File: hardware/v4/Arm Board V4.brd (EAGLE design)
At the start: 108 x 50.8 mm, 38 parts, among them IC3 L6206D, P1 STELLARIS-LAUNCHPADSTELLARIS-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, U1 SN74LS241DW, U2 XBEE-1B3

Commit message: cleaned up robo arm a bit
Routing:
- net A1: track 31.0 -> 31.9 mm
- net GND: track 16.8 -> 17.6 mm, vias 8 -> 10
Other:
- board text added: "5V"
- board text added: "GND"
- board text added: "RX3"
- board text added: "TX3"
- board text removed: "GND 5V RX3 TX3"

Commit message: added cap
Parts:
- added C1: (no value), SparkFun-Capacitors:PANASONIC_E
- moved JP11 2.54 mm to (86.8, 46.2)
- moved JP12 2.54 mm to (98.3, 46.2)
- moved JP10 2.54 mm to (92.6, 46.2)
- moved U$7 1.37 mm to (66.0, 46.4)
- moved JP9 0.78 mm to (79.2, 46.6), turned to 180 degrees
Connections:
- net +12V: now also C1.+
- net GND: now also C1.-
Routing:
- net DDATA_1: track 108.3 -> 84.0 mm
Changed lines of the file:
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@@
 </element>
 <element name="U2" library="SparkFun" package="XBEE-SMD" value="XBEE-1B3" x="59.37" y="0"/>
-<element name="JP9" library="MRDT-2015-Arm" package="DYNAMIXEL-1X03" value="DYNAMIXEL-1X03" x="78.58125" y="46.19625" smashed="yes" rot="R270">
-<attribute name="NAME" x="80.41005" y="47.54245" size="1.27" layer="25" ratio="10" rot="R270" display="off"/>
-<attribute name="VALUE" x="75.40625" y="47.46625" size="1.27" layer="27" rot="R270"/>
-</element>
-<element name="JP10" library="MRDT-2015-Arm" package="DYNAMIXEL-1X03" value="DYNAMIXEL-1X03" x="90.01125" y="46.19625" smashed="yes" rot="R270">
-<attribute name="NAME" x="91.84005" y="47.54245" size="1.27" layer="25" ratio="10" rot="R270" display="off"/>
-<attribute name="VALUE" x="86.83625" y="47.46625" size="1.27" layer="27" rot="R270"/>
-</element>
-<element name="JP11" library="MRDT-2015-Arm" package="DYNAMIXEL-1X03" value="DYNAMIXEL-1X03" x="84.29625" y="46.19625" smashed="yes" rot="R270">
-<attribute name="NAME" x="86.12505" y="47.54245" size="1.27" layer="25" ratio="10" rot="R270" display="off"/>
-<attribute name="VALUE" x="81.12125" y="47.46625" size="1.27" layer="27" rot="R270"/>
-</element>
-<element name="JP12" library="MRDT-2015-Arm" package="DYNAMIXEL-1X03" value="DYNAMIXEL-1X03" x="95.72625" y="46.19625" smashed="yes" rot="R270">
-<attribute name="NAME" x="97.55505" y="47.54245" size="1.27" layer="25" ratio="10" rot="R270" display="off"/>
-<attribute name="VALUE" x="92.55125" y="47.46625" size="1.27" layer="27" rot="R270"/>
+<element name="JP9" library="MRDT-2015-Arm" package="DYNAMIXEL-1X03" value="DYNAMIXEL-1X03" x="79.21625" y="46.64075" smashed="yes" rot="R180">
+<attribute name="NAME" x="80.56245" y="44.81195" size="1.27" layer="25" ratio="10" rot="R180" display="off"/>
+<attribute name="VALUE" x="80.48625" y="49.81575" size="1.27" layer="27" rot="R180"/>
+</element>
+<element name="JP10" library="MRDT-2015-Arm" package="DYNAMIXEL-1X03" value="DYNAMIXEL-1X03" x="92.55125" y="46.19625" smashed="yes" rot="R270">
+<attribute name="NAME" x="94.38005" y="47.54245" size="1.27" layer="25" ratio="10" rot="R270" display="off"/>
+<attribute name="VALUE" x="89.37625" y="47.46625" size="1.27" layer="27" rot="R270"/>
+</element>
+<element name="JP11" library="MRDT-2015-Arm" package="DYNAMIXEL-1X03" value="DYNAMIXEL-1X03" x="86.83625" y="46.19625" smashed="yes" rot="R270">
+<attribute name="NAME" x="88.66505" y="47.54245" size="1.27" layer="25" ratio="10" rot="R270" display="off"/>
+<attribute name="VALUE" x="83.66125" y="47.46625" size="1.27" layer="27" rot="R270"/>
+</element>
+<element name="JP12" library="MRDT-2015-Arm" package="DYNAMIXEL-1X03" value="DYNAMIXEL-1X03" x="98.26625" y="46.19625" smashed="yes" rot="R270">
+<attribute name="NAME" x="100.09505" y="47.54245" size="1.27" layer="25" ratio="10" rot="R270" display="off"/>
+<attribute name="VALUE" x="95.09125" y="47.46625" size="1.27" layer="27" rot="R270"/>
 </element>
 <element name="P1" library="StellarisLaunchPad_Fred" package="LAUNCHPAD-XL" value="STELLARIS-LAUNCHPADSTELLARIS-LAUNCHPAD-XL" x="-21.59" y="0"/>
@@
 <element name="S3" library="SparkFun-Electromechanical" package="STANDOFF-ELECTRICAL" value="STANDOFF_ELECTRICAL" x="100.33" y="8.89" rot="MR0"/>
 <element name="S4" library="SparkFun-Electromechanical" package="STANDOFF-ELECTRICAL" value="STANDOFF_ELECTRICAL" x="104.14" y="46.99"/>
-<element name="U$7" library="MRDT-2015-PowerBoard" package="691321100002" value="H_WR-TBL_321*0002VERT" x="66.4845" y="45.085" smashed="yes">
-<attribute name="DIGIKEY_PN" value="732-2763-ND" x="66.4845" y="45.085" size="1.778" layer="27" display="off"/>
+<element name="U$7" library="MRDT-2015-PowerBoard" package="691321100002" value="H_WR-TBL_321*0002VERT" x="65.9765" y="46.355" smashed="yes">
+<attribute name="DIGIKEY_PN" value="732-2763-ND" x="65.9765" y="46.355" size="1.778" layer="27" display="off"/>
 </element>
 <element name="JP1" library="SparkFun-Connectors" package="1X04" value="" x="55.88" y="3.81" smashed="yes">
@@
 <attribute name="DIGIKEY_PN" value="732-2763-ND" x="112.776" y="41.402" size="1.778" layer="27" rot="R270" display="off"/>
 </element>
+<element name="C1" library="SparkFun-Capacitors" package="PANASONIC_E" value="" x="73.914" y="55.372" rot="R90"/>
 </elements>
 <signals>
@@
 <via x="95.377" y="19.304" extent="1-16" drill="0.5"/>
 <wire x1="95.377" y1="18.514" x2="95.377" y2="19.304" width="0.4064" layer="1"/>
+<contactref element="C1" pad="-"/>
+<wire x1="79.21625" y1="46.64075" x2="73.914" y2="52.372" width="0" layer="19" extent="1-1"/>
 </signal>
 <signal name="+3V3">
@@
 <vertex x="71.12" y="39.624"/>
 <vertex x="74.168" y="42.672"/>
-<vertex x="97.028" y="42.672"/>
-<vertex x="99.568" y="40.132"/>
+<vertex x="99.568" y="42.672"/>
 <vertex x="99.568" y="28.956"/>
 <vertex x="88.646" y="28.956"/>
@@
 <wire x1="89.024" y1="25.4" x2="88.9" y2="25.4" width="0.4064" layer="16"/>
 <contactref element="U$1" pad="VIN"/>
+<contactref element="C1" pad="+"/>
+<wire x1="76.67625" y1="46.64075" x2="73.914" y2="58.372" width="0" layer="19" extent="1-1"/>
 </signal>
 <signal name="RST">
@@
 <contactref element="JP11" pad="DDATA"/>
 <contactref element="JP12" pad="DDATA"/>
-<wire x1="95.72625" y1="41.11625" x2="90.01125" y2="41.11625" width="0.4064" layer="1"/>
-<wire x1="90.01125" y1="41.11625" x2="84.29625" y2="41.11625" width="0.4064" layer="1"/>
 <contactref element="JP9" pad="DDATA"/>
-<wire x1="84.29625" y1="41.11625" x2="78.58125" y2="41.11625" width="0.4064" layer="1"/>
 <contactref element="U1" pad="2"/>
 <contactref element="U1" pad="3"/>
@@
 <wire x1="72.39" y1="25.146" x2="72.39" y2="38.862" width="0.4064" layer="1"/>
 <wire x1="16.38935" y1="14.85265" x2="16.51" y2="14.85265" width="0.4064" layer="1"/>
-<wire x1="72.39" y1="38.862" x2="74.676" y2="41.148" width="0.4064" layer="1"/>
-<wire x1="74.676" y1="41.148" x2="78.5495" y2="41.148" width="0.4064" layer="1"/>
-<wire x1="78.5495" y1="41.148" x2="78.58125" y2="41.11625" width="0.4064" layer="1"/>
 <contactref element="D1" pad="C"/>
 <wire x1="16.38935" y1="14.85265" x2="15.24" y2="14.85265" width="0.4064" layer="1"/>
 <wire x1="72.39" y1="38.862" x2="72.366" y2="38.862" width="0.4064" layer="1"/>
+<wire x1="92.55125" y1="41.11625" x2="98.26625" y2="41.11625" width="0" layer="19" extent="1-1"/>
+<wire x1="86.83625" y1="41.11625" x2="92.55125" y2="41.11625" width="0" layer="19" extent="1-1"/>
+<wire x1="74.13625" y1="46.64075" x2="86.83625" y2="41.11625" width="0" layer="19" extent="1-1"/>
+<wire x1="72.366" y1="38.862" x2="74.13625" y2="46.64075" width="0" layer="19" extent="1-1"/>
 </signal>
 <signal name="N$7">

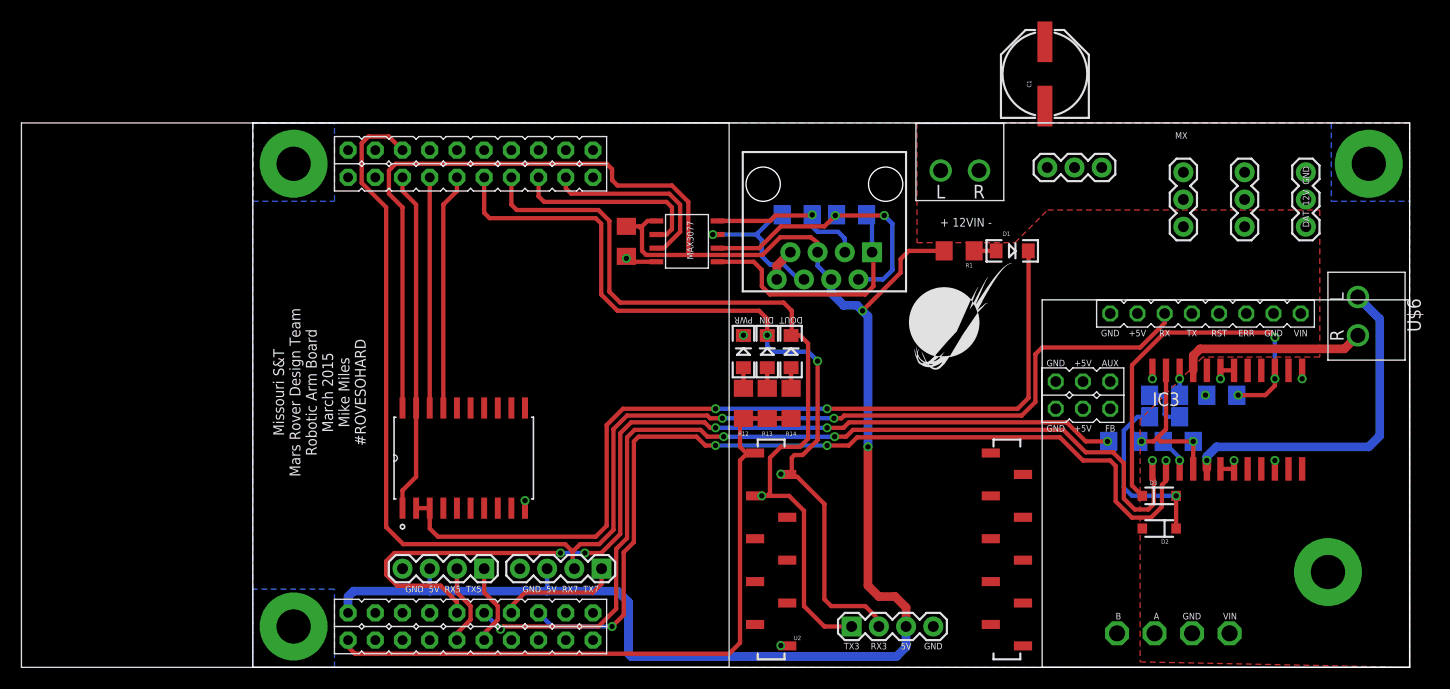
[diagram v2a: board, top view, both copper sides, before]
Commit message: added cap, rerouted
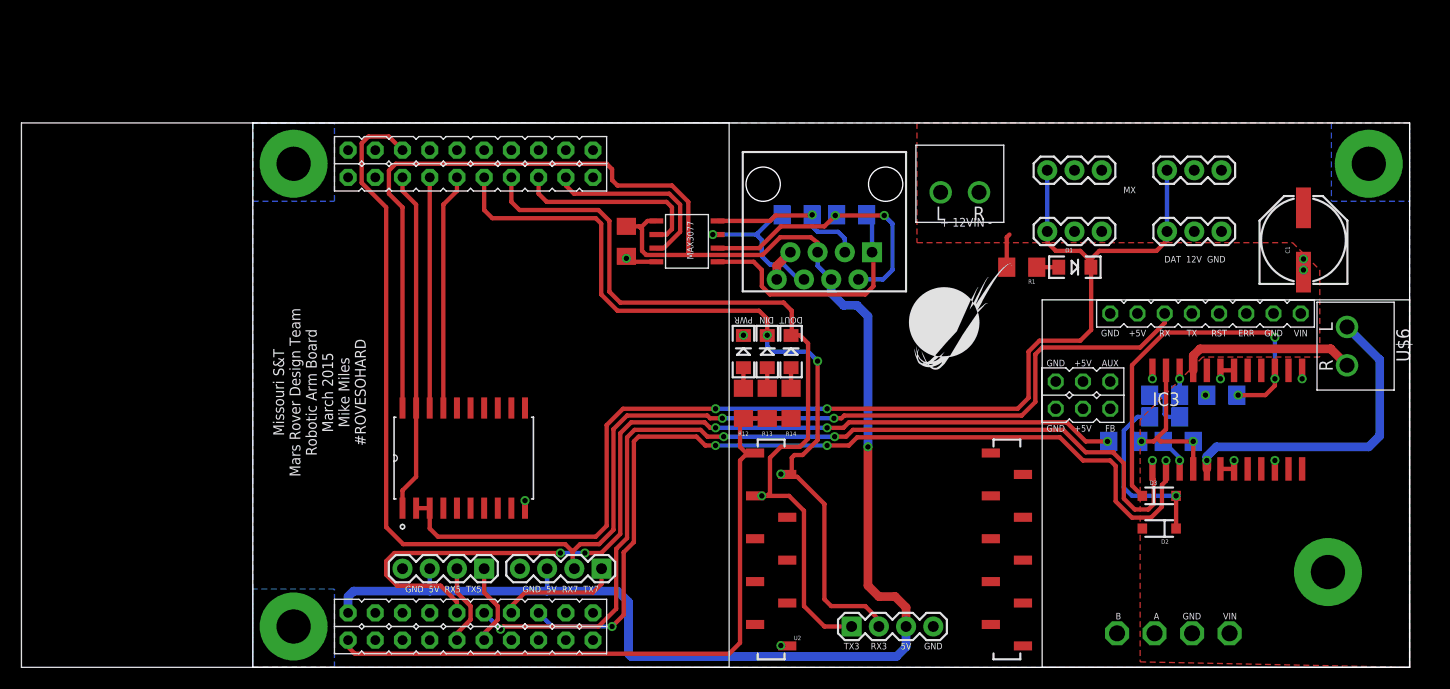
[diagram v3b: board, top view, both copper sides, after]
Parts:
- C1: value (none) -> 330uF
- moved C1 28.7 mm to (98.0, 39.9)
- moved JP12 9.62 mm to (90.4, 40.7), turned to 180 degrees
- moved JP11 9.41 mm to (79.2, 40.7), turned to 180 degrees
- moved D1 6.04 mm to (76.7, 37.3)
- moved R1 6.04 mm to (71.8, 37.3)
- moved U$6 2.97 mm to (102.1, 30.0)
- moved JP10 2.17 mm to (90.4, 46.4), turned to 180 degrees
- moved U$7 2.03 mm to (66.0, 44.3)
- moved JP9 0.25 mm to (79.2, 46.4)
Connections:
- net +12V: now also R1.2
- net +5V: no longer R1.2
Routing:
- net DDATA_1: track 84.0 -> 113.8 mm
- net +5V: track 198.0 -> 187.3 mm, vias 2 -> 1
- net +12V: track 0.12 -> 3.28 mm
- net A1: track 31.9 -> 29.5 mm
- net GND: track 17.6 -> 18.8 mm, vias 10 -> 12
- net A2: track 17.5 -> 16.6 mm

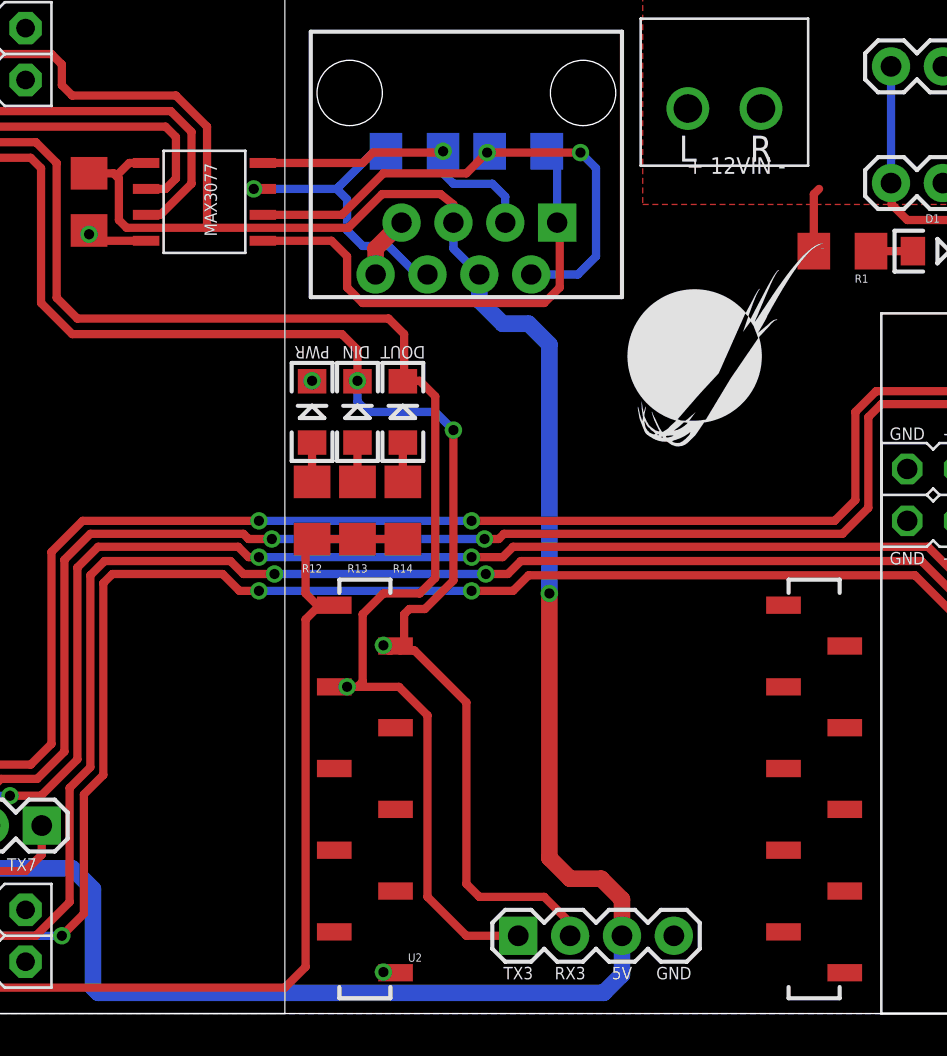
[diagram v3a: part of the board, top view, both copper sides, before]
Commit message: reroute ethernet port
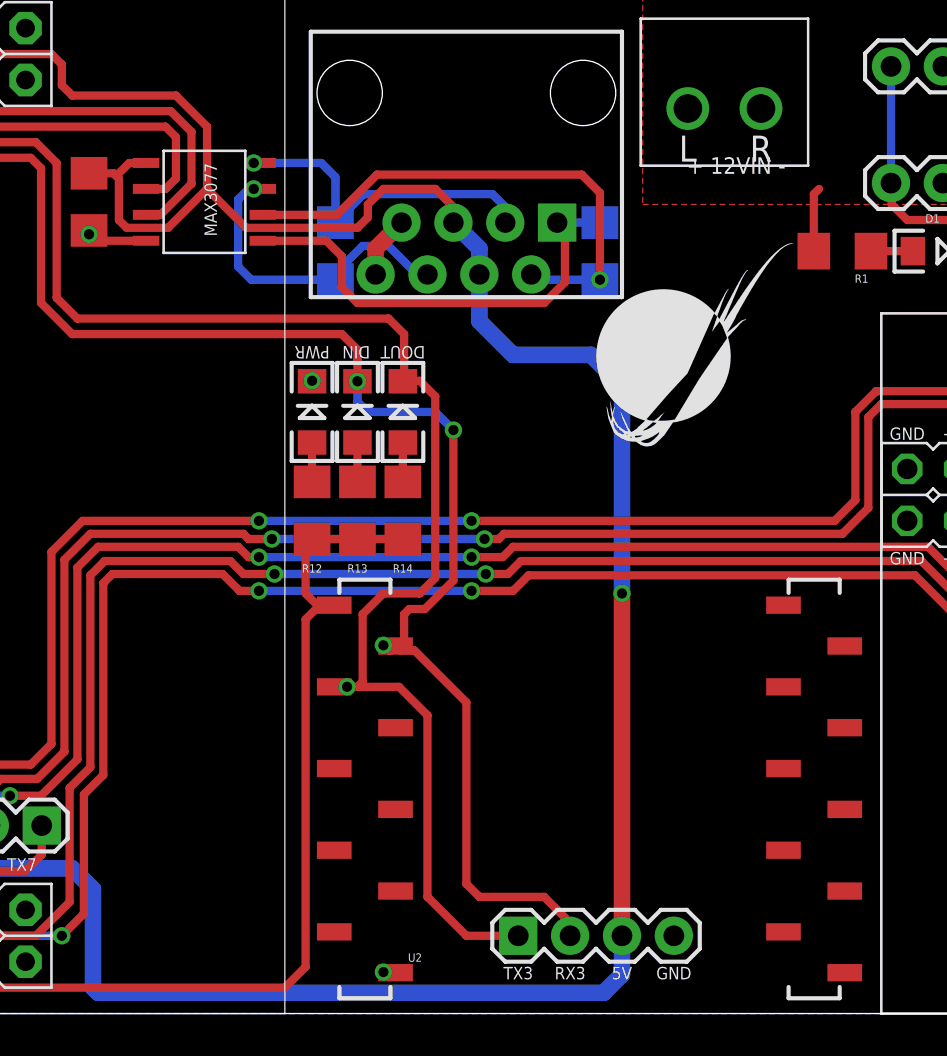
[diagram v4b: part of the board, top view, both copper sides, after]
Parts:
- moved R11 6.32 mm to (59.9, 37.3), turned to 90 degrees
- moved R10 6.24 mm to (46.9, 37.3), turned to 270 degrees
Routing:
- net N$3: track 14.9 -> 16.9 mm
- net N$5: track 23.9 -> 22.5 mm
- net N$2: track 14.8 -> 15.7 mm
- net +5V: track 187.3 -> 188.1 mm
- net N$1: track 26.2 -> 25.4 mm, vias 2 -> 1

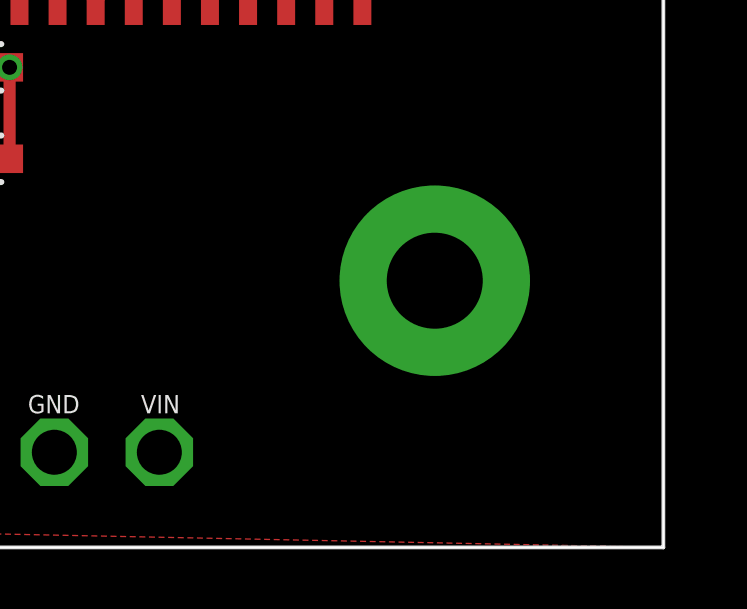
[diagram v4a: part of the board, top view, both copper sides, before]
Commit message: cleaned up brd, updated bom
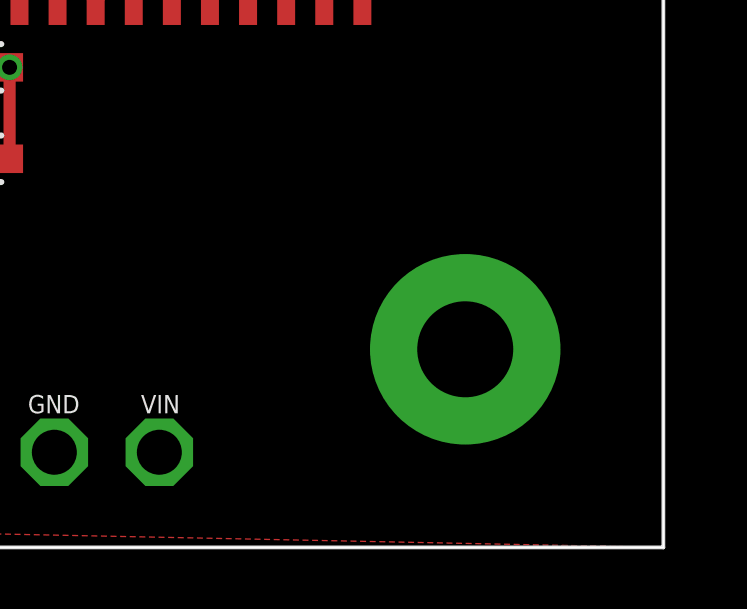
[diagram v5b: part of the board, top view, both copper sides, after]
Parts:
- moved S3 2.50 mm to (101.3, 6.60)
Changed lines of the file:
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@@
 <layer number="223" name="223bmp" color="24" fill="1" visible="no" active="no"/>
 <layer number="224" name="224bmp" color="25" fill="1" visible="no" active="no"/>
+<layer number="225" name="225bmp" color="7" fill="1" visible="yes" active="yes"/>
+<layer number="226" name="226bmp" color="7" fill="1" visible="yes" active="yes"/>
+<layer number="227" name="227bmp" color="7" fill="1" visible="yes" active="yes"/>
+<layer number="228" name="228bmp" color="7" fill="1" visible="yes" active="yes"/>
+<layer number="229" name="229bmp" color="7" fill="1" visible="yes" active="yes"/>
+<layer number="230" name="230bmp" color="7" fill="1" visible="yes" active="yes"/>
 <layer number="231" name="Eagle3D_PG1" color="7" fill="1" visible="no" active="no"/>
 <layer number="232" name="Eagle3D_PG2" color="7" fill="1" visible="no" active="no"/>
@@
 <layer number="251" name="SMDround" color="12" fill="11" visible="no" active="no"/>
 <layer number="254" name="cooling" color="7" fill="1" visible="no" active="no"/>
+<layer number="255" name="routoute" color="7" fill="1" visible="yes" active="yes"/>
 </layers>
 <board>
@@
 </autorouter>
 <elements>
-<element name="U$3" library="SparkFun-Connectors" package="RJ45-8" value="RJ45-8PTH" x="53.34" y="45.085" rot="R180"/>
+<element name="U$3" library="SparkFun-Connectors" package="RJ45-8" value="RJ45-8PTH" x="53.34" y="45.085" rot="R180">
+<attribute name="PROD_ID" value="CONN-08506" x="53.34" y="45.085" size="1.778" layer="27" rot="R180" display="off"/>
+<attribute name="VALUE" value="RJ45" x="53.34" y="45.085" size="1.778" layer="27" rot="R180" display="off"/>
+</element>
 <element name="R10" library="SparkFun-Passives" package="1206" value="120 Ohm" x="46.9265" y="37.338" smashed="yes" rot="MR270">
 <attribute name="NAME" x="45.7835" y="37.338" size="0.4064" layer="26" font="vector" rot="MR270" align="bottom-center"/>
@@
 <element name="S1" library="SparkFun-Electromechanical" package="STANDOFF-ELECTRICAL" value="STANDOFF_ELECTRICAL" x="3.81" y="3.81"/>
 <element name="S2" library="SparkFun-Electromechanical" package="STANDOFF-ELECTRICAL" value="STANDOFF_ELECTRICAL" x="3.81" y="46.99"/>
-<element name="S3" library="SparkFun-Electromechanical" package="STANDOFF-ELECTRICAL" value="STANDOFF_ELECTRICAL" x="100.33" y="8.89" rot="MR0"/>
+<element name="S3" library="SparkFun-Electromechanical" package="STANDOFF-ELECTRICAL" value="STANDOFF_ELECTRICAL" x="101.346" y="6.604" rot="MR0"/>
 <element name="S4" library="SparkFun-Electromechanical" package="STANDOFF-ELECTRICAL" value="STANDOFF_ELECTRICAL" x="104.14" y="46.99"/>
 <element name="U$7" library="MRDT-2015-PowerBoard" package="691321100002" value="H_WR-TBL_321*0002VERT" x="65.9765" y="44.323" smashed="yes">
@@
 <signal name="GND">
 <contactref element="C12" pad="2"/>
-<contactref element="U$3" pad="8"/>
-<contactref element="U$3" pad="7"/>
 <contactref element="LED1" pad="C"/>
 <contactref element="U2" pad="10"/>
@@
 <wire x1="98.044" y1="36.878" x2="98.044" y2="38.1" width="0.4064" layer="1"/>
 <via x="98.044" y="37.084" extent="1-16" drill="0.5"/>
+<contactref element="U$3" pad="8"/>
+<contactref element="U$3" pad="7"/>
 <wire x1="48.895" y1="36.195" x2="48.895" y2="37.465" width="0.8128" layer="1"/>
 <wire x1="48.895" y1="37.465" x2="50.165" y2="38.735" width="0.8128" layer="1"/>
